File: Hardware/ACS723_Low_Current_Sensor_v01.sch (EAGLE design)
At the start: 19 parts, among them U1 ACS712, U2 OPA344

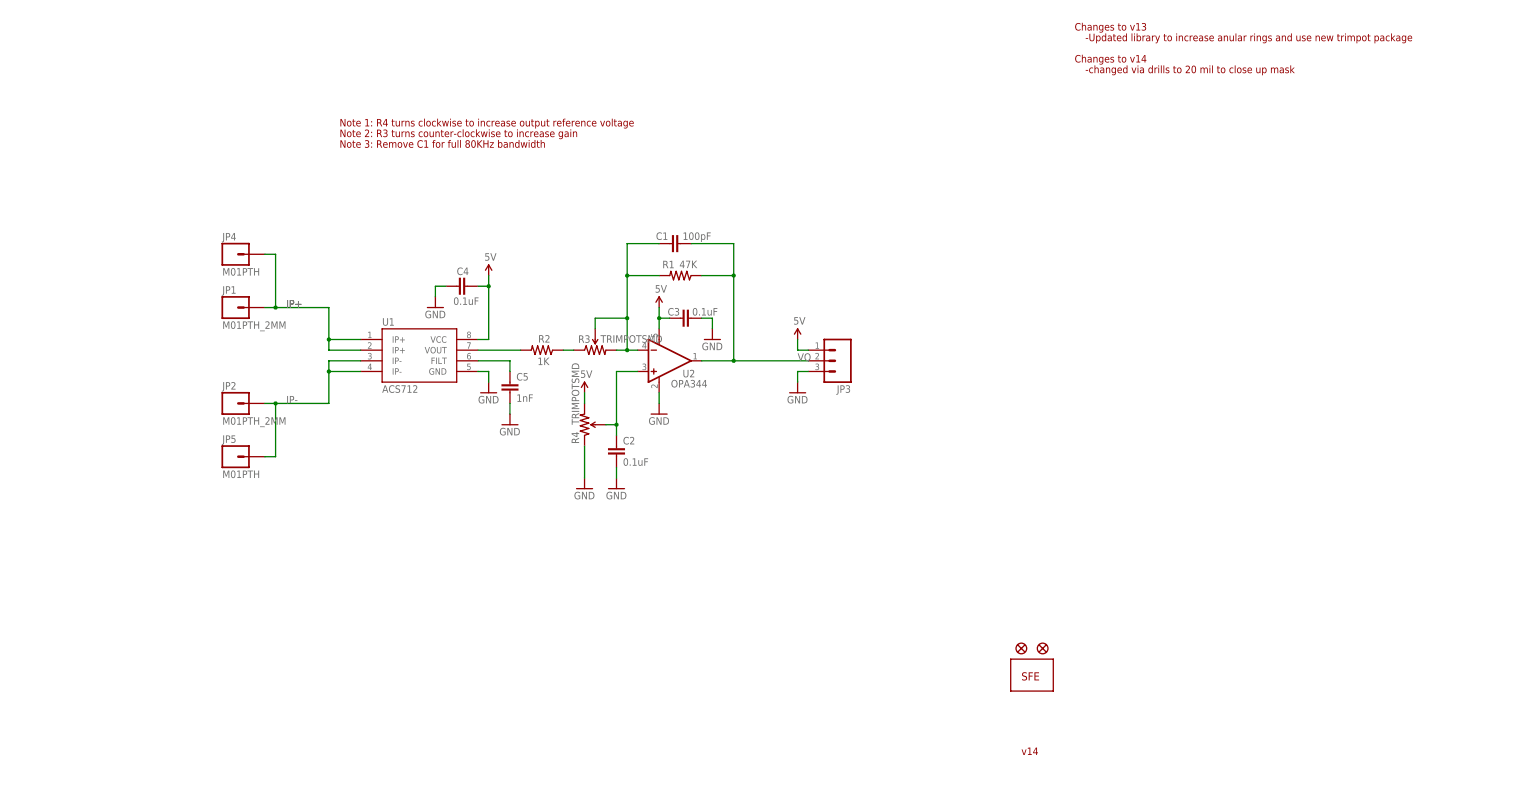
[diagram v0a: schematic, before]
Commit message: Rerouting and deletion of original files
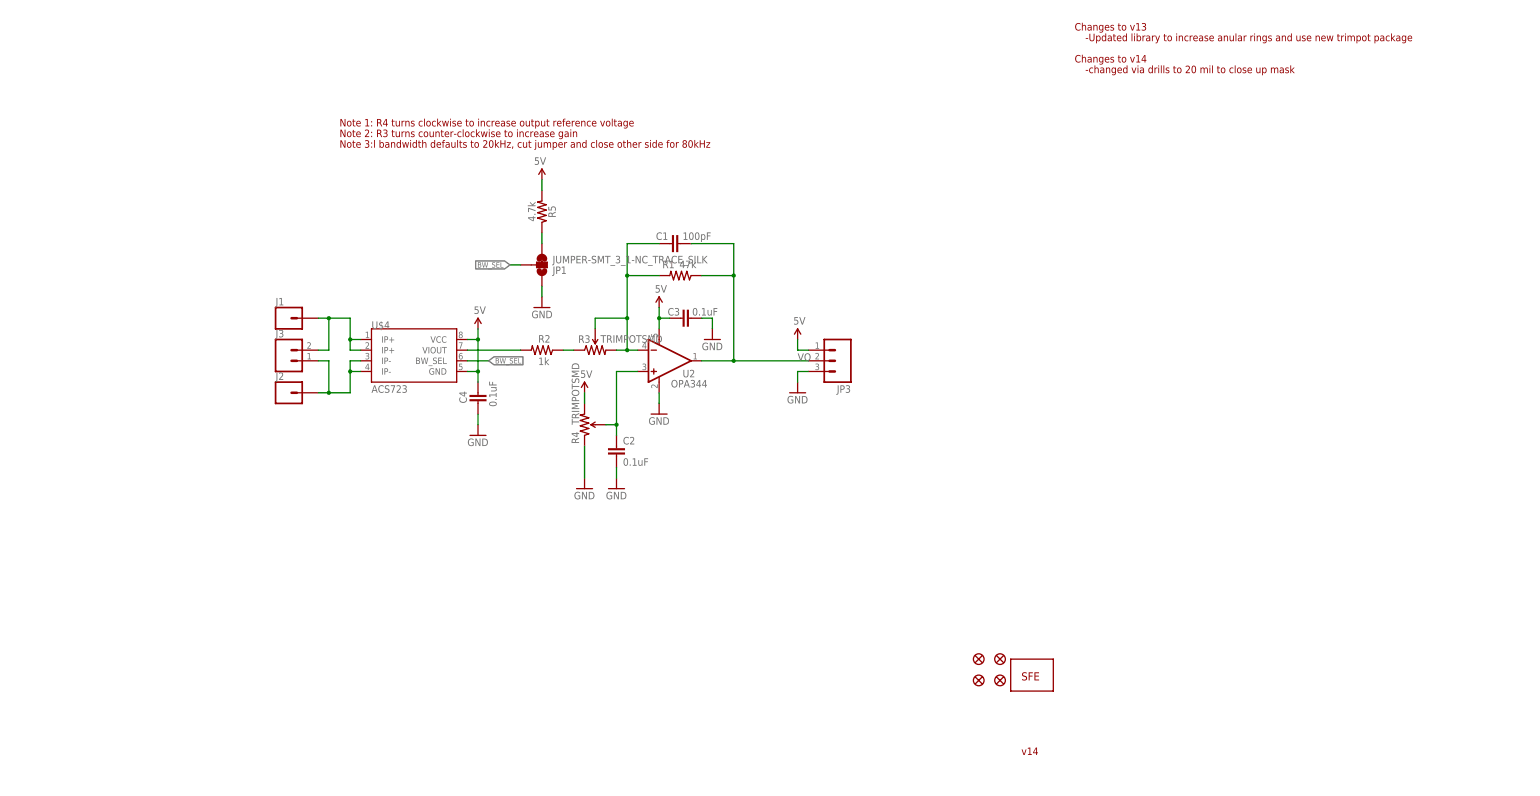
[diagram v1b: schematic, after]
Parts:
- removed C5: 1nF, SparkFun:CAP0402-CAP
- removed JP2: M01PTH_2MM, SparkFun:M01PTH_2MM
- removed JP4, JP5: M01PTH, SparkFun:M01PTH
- removed U$1, U$3: FIDUCIALUFIDUCIAL, SparkFun:FIDUCIALUFIDUCIAL
- removed U1: ACS712, SparkFun:ACS712
- added FD1, FD2, FD3, FD4: FIDUCIAL1X2, SparkFun-Aesthetics:FIDUCIAL1X2
- added J1, J2: (no value), SparkFun-Connectors:CONN_01SMTSO-256-ET-0.165DIA
- added J3: (no value), SparkFun-Connectors:CONN_021X02_NO_SILK
- added R5: 4.7k, SparkFun-Resistors:4.7KOHM-0603-1/10W-1%
- added U$4: ACS723, SparkFun-IC-Power:ACS723
- C1: device SparkFun:CAP0402-CAP -> SparkFun-Capacitors:100PF-0603-50V-5%
- C2, C3, C4: device SparkFun:CAP0402-CAP -> SparkFun-Capacitors:0.1UF-0603-25V-(+80/-20%)
- JP1: value M01PTH_2MM -> JUMPER-SMT_3_1-NC_TRACE_SILK; device SparkFun:M01PTH_2MM -> SparkFun-Jumpers:JUMPER-SMT_3_1-NC_TRACE_SILK
- R1: value 47K -> 47k; device SparkFun:RESISTOR0402-RES -> SparkFun-Resistors:47KOHM-0603-1/10W-1%
- R2: value 1K -> 1k; device SparkFun:RESISTOR0402-RES -> SparkFun-Resistors:1KOHM-0603-1/10W-1%
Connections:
- removed net N$8: C5.1, U1.FILT
- new net BW_SEL: JP1.2, U$4.BW_SEL
- new net N$1: JP1.3, R5.1
- net 5V: now also R5.2, U$4.GND, U$4.VCC; no longer U1.VCC
- net GND: now also JP1.1; no longer C5.2, U1.GND
- net IP+: now also J1.1, J3.2, U$4.IP+@1, U$4.IP+@2; no longer JP1.1, JP4.1, U1.IP+@1, U1.IP+@2
- net IP-: now also J2.1, J3.1, U$4.IP-@1, U$4.IP-@2; no longer JP2.1, JP5.1, U1.IP-@3, U1.IP-@4
- net N$3: now also U$4.VIOUT; no longer U1.VOUT
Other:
- note added: "Note 3:l bandwidth defaults to 20kHz, cut jumper and close other side for 80kHz"
- note removed: "Note 3: Remove C1 for full 80KHz bandwidth"
- moved on the sheet: C4

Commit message: Finalizing v01
-reduced GND plane to isolate from IP pins
-swapped all existing 0402 packages to 0603
-updated trimpot packages
-added extra copper for large IP traces on bottom copper
-added bandwidth select jumper
-swapped in new opamp symbol and package
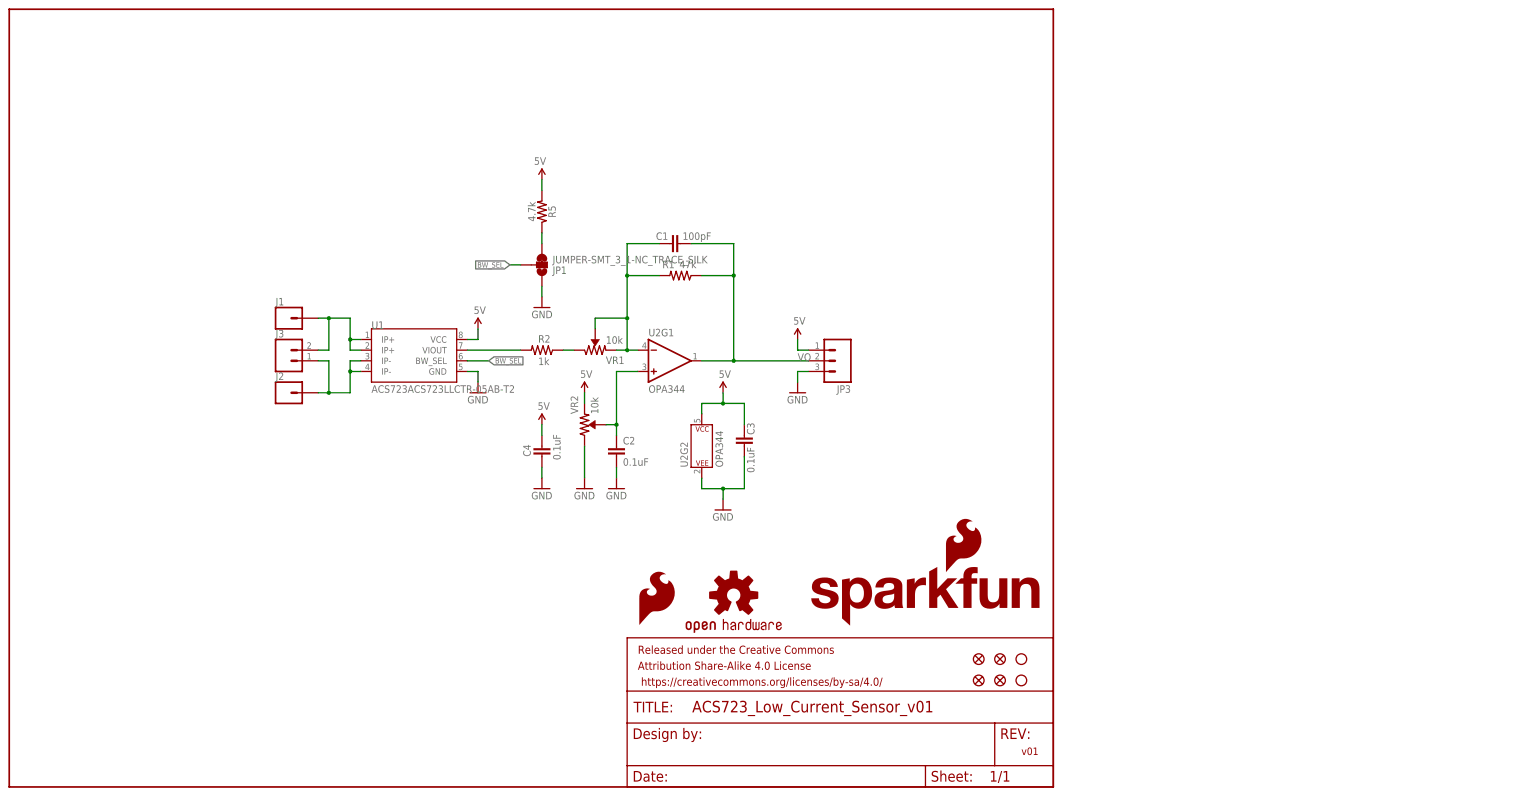
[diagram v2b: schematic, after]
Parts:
- removed R3, R4: TRIMPOTSMD, SparkFun:TRIMPOTSMD
- removed U$2: LOGO-SFENEW, SparkFun:LOGO-SFENEW
- removed U$4: ACS723, SparkFun-IC-Power:ACS723
- added FRAME1: FRAME-LETTER, SparkFun-Aesthetics:FRAME-LETTER
- added H1, H2: STAND-OFFTIGHT, SparkFun-Hardware:STAND-OFFTIGHT
- added LOGO1: SFE_LOGO_NAME_FLAME.1_INCH, SparkFun-Aesthetics:SFE_LOGO_NAME_FLAME.1_INCH
- added LOGO2: OSHW-LOGOS, SparkFun-Aesthetics:OSHW-LOGOS
- added LOGO3: SFE_LOGO_FLAME.1_INCH, SparkFun-Aesthetics:SFE_LOGO_FLAME.1_INCH
- added U1: ACS723ACS723LLCTR-05AB-T2, SparkFun-IC-Power:ACS723ACS723LLCTR-05AB-T2
- added VR1, VR2: 10k, SparkFun-Resistors:TRIMPOT-SMD-3MM-OPEN-1/10W-25%
- U2: device SparkFun:OPA344 -> SparkFun-IC-Amplifiers:OPA344
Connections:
- net 5V: now also U1.VCC, U2G2.P$V+, VR2.CCW; no longer R4.CW, U$4.GND, U$4.VCC, U2.V+
- net BW_SEL: now also U1.BW_SEL; no longer U$4.BW_SEL
- net GND: now also U1.GND, U2G2.P$V-, VR2.CW; no longer R4.CCW, U2.V-
- net IP+: now also U1.IP+@1, U1.IP+@2; no longer U$4.IP+@1, U$4.IP+@2
- net IP-: now also U1.IP-@1, U1.IP-@2; no longer U$4.IP-@1, U$4.IP-@2
- net N$3: now also U1.VIOUT; no longer U$4.VIOUT
- net N$4: now also VR1.CW; no longer R3.CCW
- net N$5: now also U2G1.-IN, VR1.CCW, VR1.WIPER; no longer R3.CW, R3.WIPER, U2.-IN
- net N$6: now also U2G1.+IN, VR2.WIPER; no longer R4.WIPER, U2.+IN
- net VO: now also U2G1.OUT; no longer U2.OUT
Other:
- note added: "v01"
- note removed: "-Updated library to increase anular rings and use new trimpot package"
- note removed: "-changed via drills to 20 mil to close up mask"
- note removed: "Changes to v13"
- note removed: "Changes to v14"
- note removed: "Note 1: R4 turns clockwise to increase output reference voltage"
- note removed: "Note 2: R3 turns counter-clockwise to increase gain"
- note removed: "Note 3:l bandwidth defaults to 20kHz, cut jumper and close other side for 80kHz"
- note removed: "v14"
- moved on the sheet: C3, C4

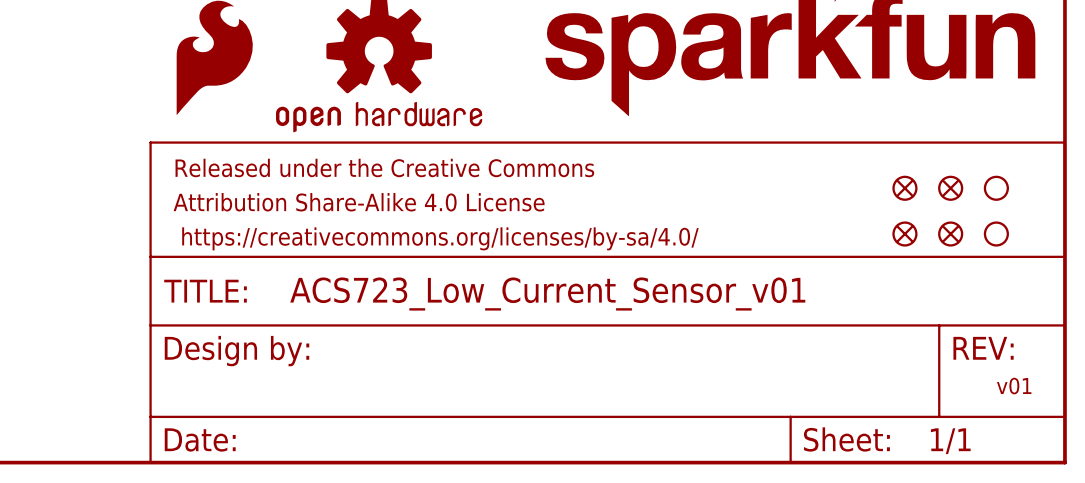
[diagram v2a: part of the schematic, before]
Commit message: Silk and designer details
-added "designed by" and "revised by" attributes in the SCH and BRD
-adjusted silk
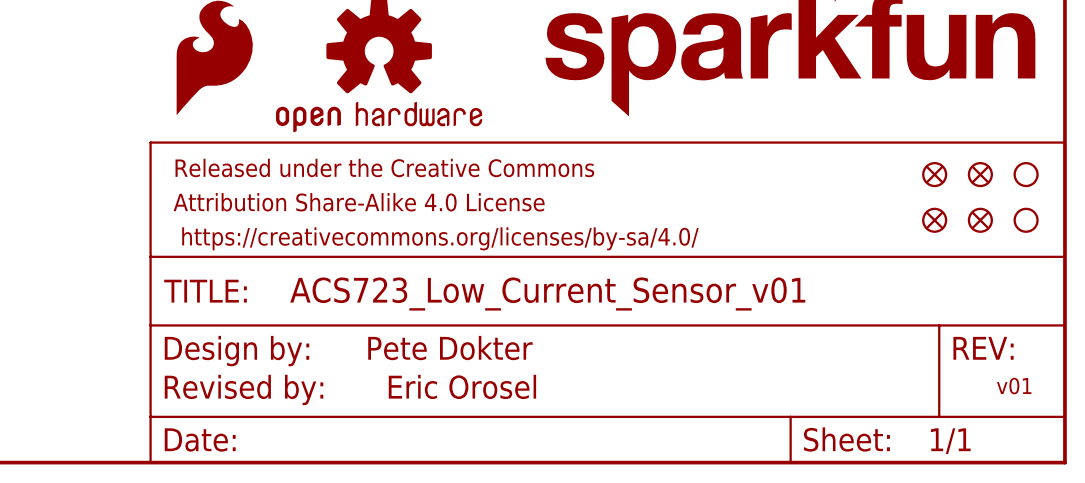
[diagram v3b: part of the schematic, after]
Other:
- note added: "Eric Orosel"
- note added: "Pete Dokter"
- note added: "Revised by:"
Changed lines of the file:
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@@
 <plain>
 <text x="241.3" y="7.62" size="1.778" layer="94">v01</text>
+<text x="171.196" y="11.43" size="2.54" layer="94">Pete Dokter</text>
+<text x="148.59" y="7.112" size="2.54" layer="94">Revised by:</text>
+<text x="173.482" y="7.112" size="2.54" layer="94">Eric Orosel</text>
 </plain>
 <instances>
@@
 <instance part="J2" gate="G$1" x="66.04" y="93.98"/>
 <instance part="J3" gate="G$1" x="66.04" y="101.6"/>
-<instance part="FD1" gate="G$1" x="236.22" y="25.4"/>
-<instance part="FD2" gate="G$1" x="231.14" y="25.4"/>
-<instance part="FD3" gate="G$1" x="231.14" y="30.48"/>
-<instance part="FD4" gate="G$1" x="236.22" y="30.48"/>
+<instance part="FD1" gate="G$1" x="239.522" y="26.924"/>
+<instance part="FD2" gate="G$1" x="234.442" y="26.924"/>
+<instance part="FD3" gate="G$1" x="234.442" y="32.004"/>
+<instance part="FD4" gate="G$1" x="239.522" y="32.004"/>
 <instance part="JP1" gate="G$1" x="127" y="124.46" rot="MR180"/>
 <instance part="GND8" gate="1" x="127" y="114.3" rot="MR0"/>
@@
 <instance part="U2" gate="G2" x="165.1" y="81.28"/>
 <instance part="GND9" gate="1" x="170.18" y="66.04"/>
-<instance part="H1" gate="G$1" x="241.3" y="25.4"/>
-<instance part="H2" gate="G$1" x="241.3" y="30.48"/>
+<instance part="H1" gate="G$1" x="244.602" y="26.924"/>
+<instance part="H2" gate="G$1" x="244.602" y="32.004"/>
 </instances>
 <busses>

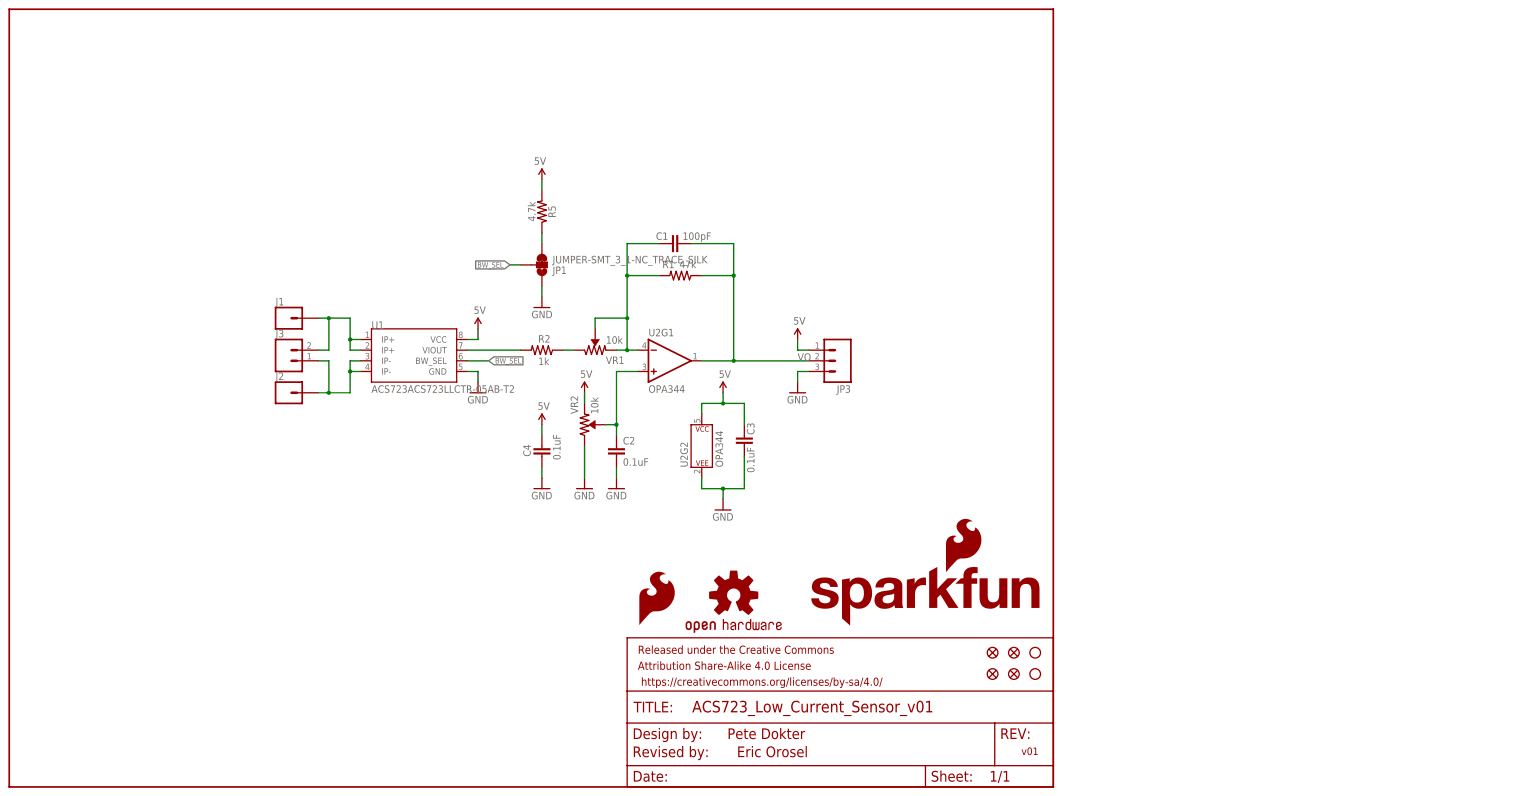
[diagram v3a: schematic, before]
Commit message: finalize for checklist
-removed oen standoff
-added 1nf cap
-moved silk
-moved header for output
-added measures
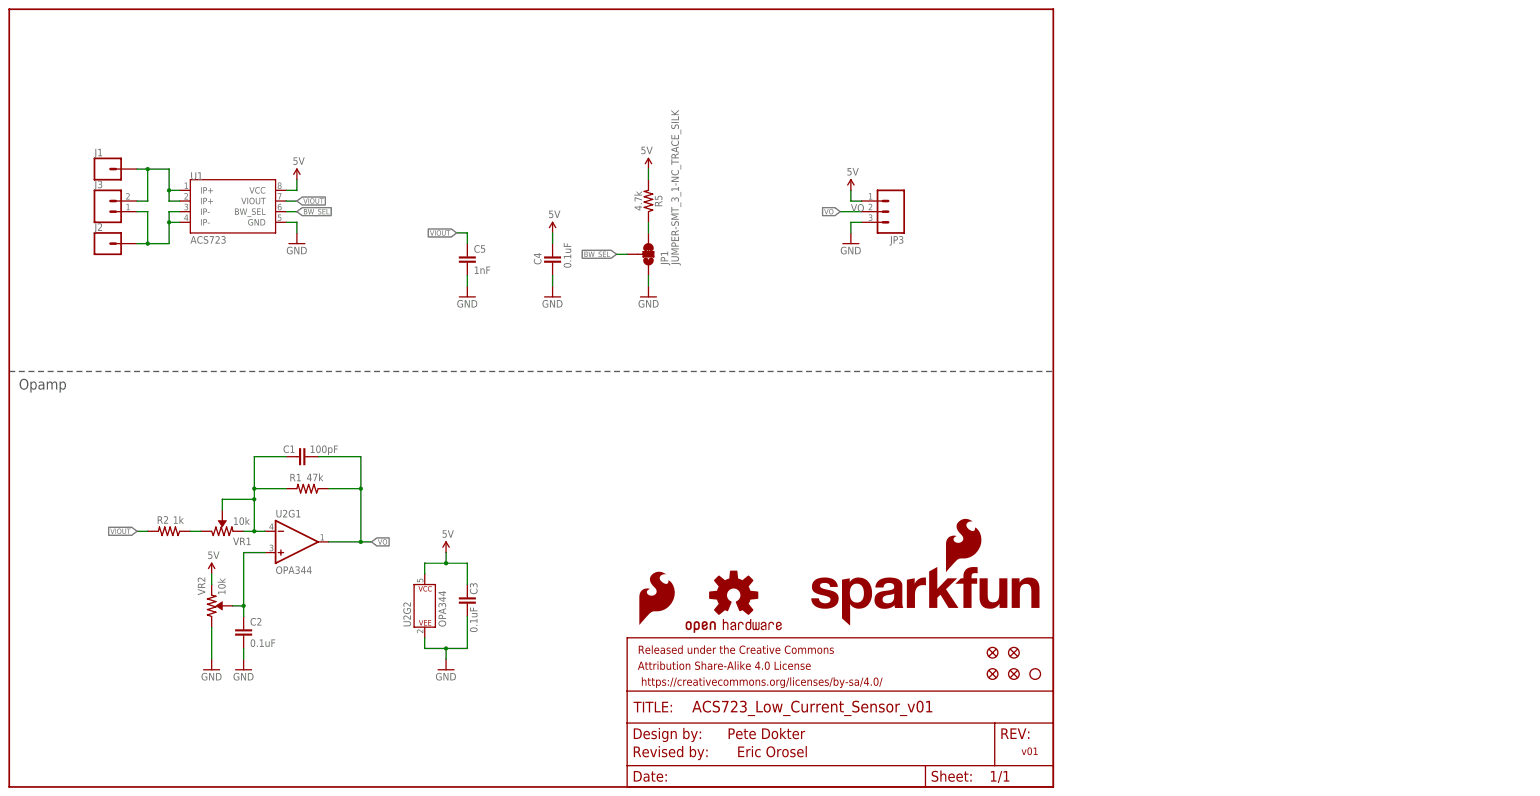
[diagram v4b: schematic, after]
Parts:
- removed H2: STAND-OFFTIGHT, SparkFun-Hardware:STAND-OFFTIGHT
- added C5: 1nF, SparkFun-Capacitors:1.0NF/1000PF-0603-50V-10%
- U1: value ACS723ACS723LLCTR-05AB-T2 -> ACS723; device SparkFun-IC-Power:ACS723ACS723LLCTR-05AB-T2 -> SparkFun-Sensors:ACS723
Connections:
- removed net N$3: R2.2, U1.VIOUT
- new net VIOUT: C5.1, R2.2, U1.VIOUT
- net GND: now also C5.2
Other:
- note added: "Opamp"
- moved on the sheet: C1, C2, C3, C4, J1, J2, J3, JP1, JP3, R1, R2, R5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
